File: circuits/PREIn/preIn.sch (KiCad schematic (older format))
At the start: 45 parts, among them K1 CONN_3, P1 CONN_1, P10 CONN_1, P11 CONN_1, P2 CONN_1, P4 CONN_1, P5 CONN_1, P6 CONN_1, P7 CONN_1, P8 CONN_1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

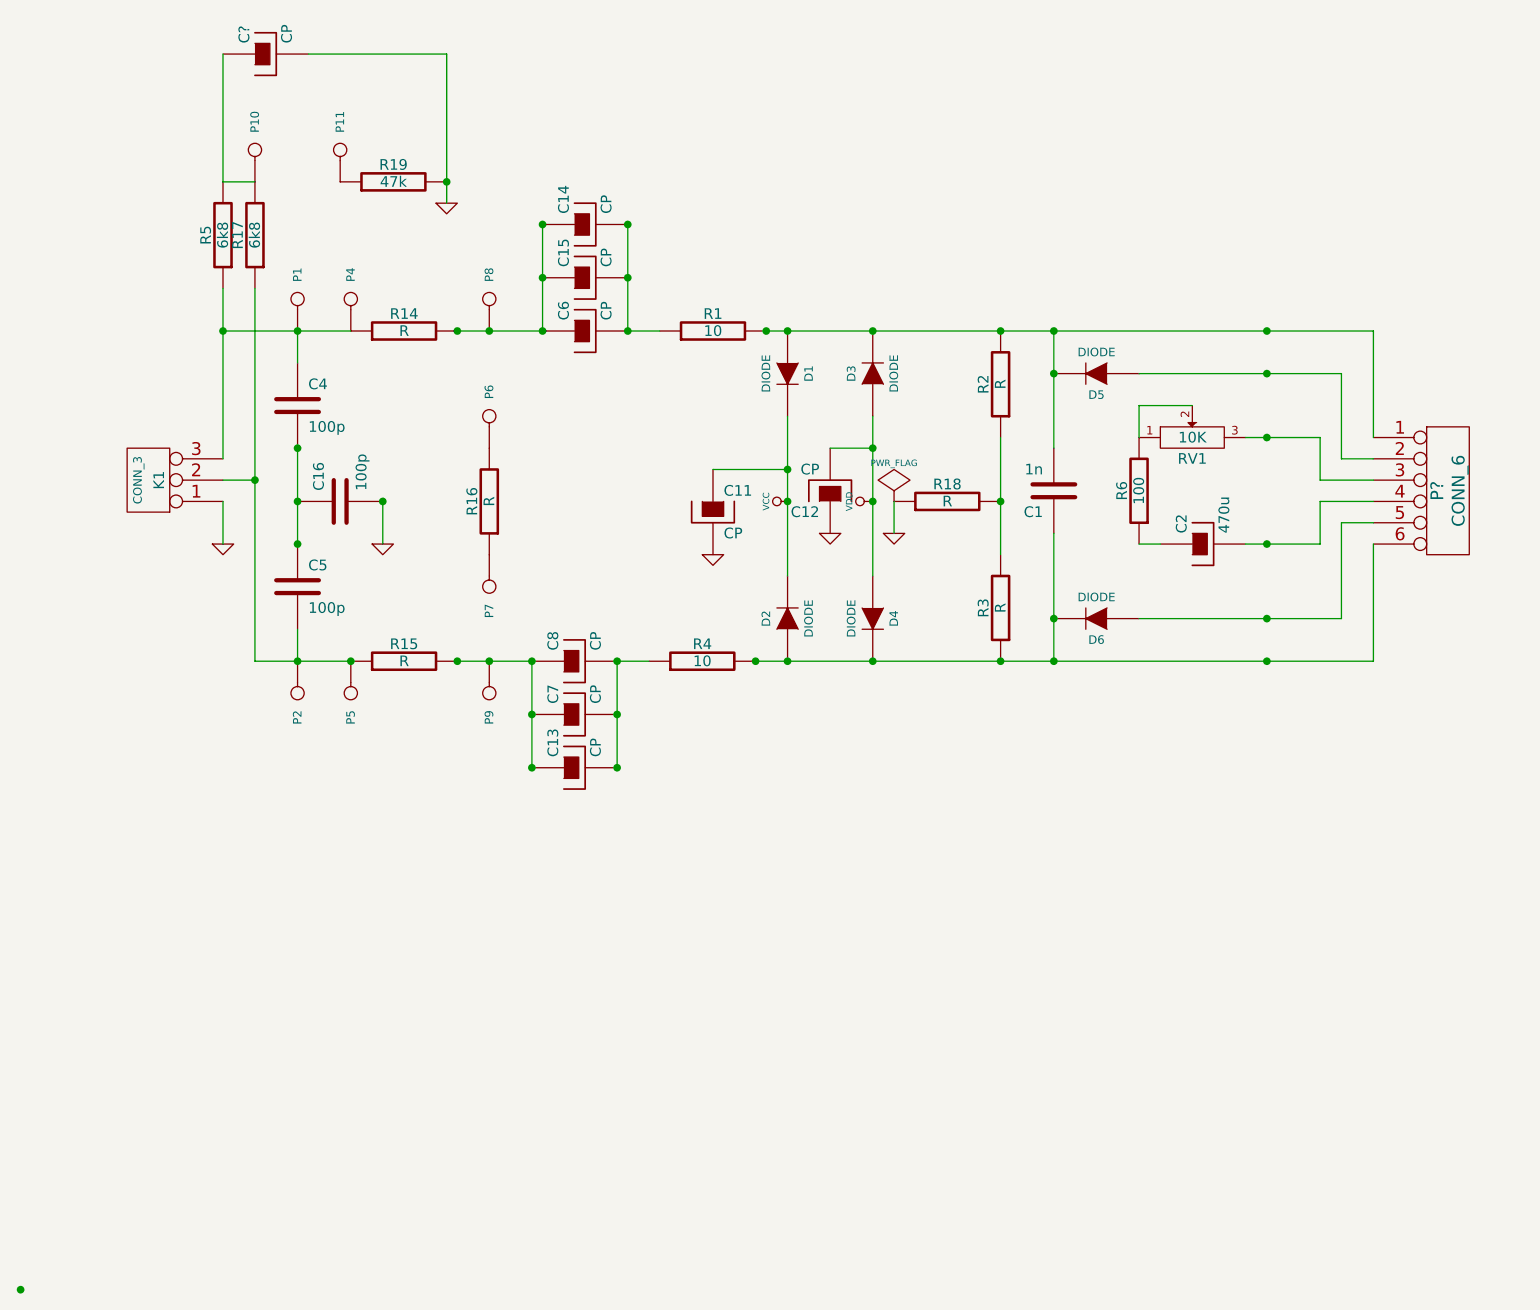
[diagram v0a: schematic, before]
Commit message: docs on transformers
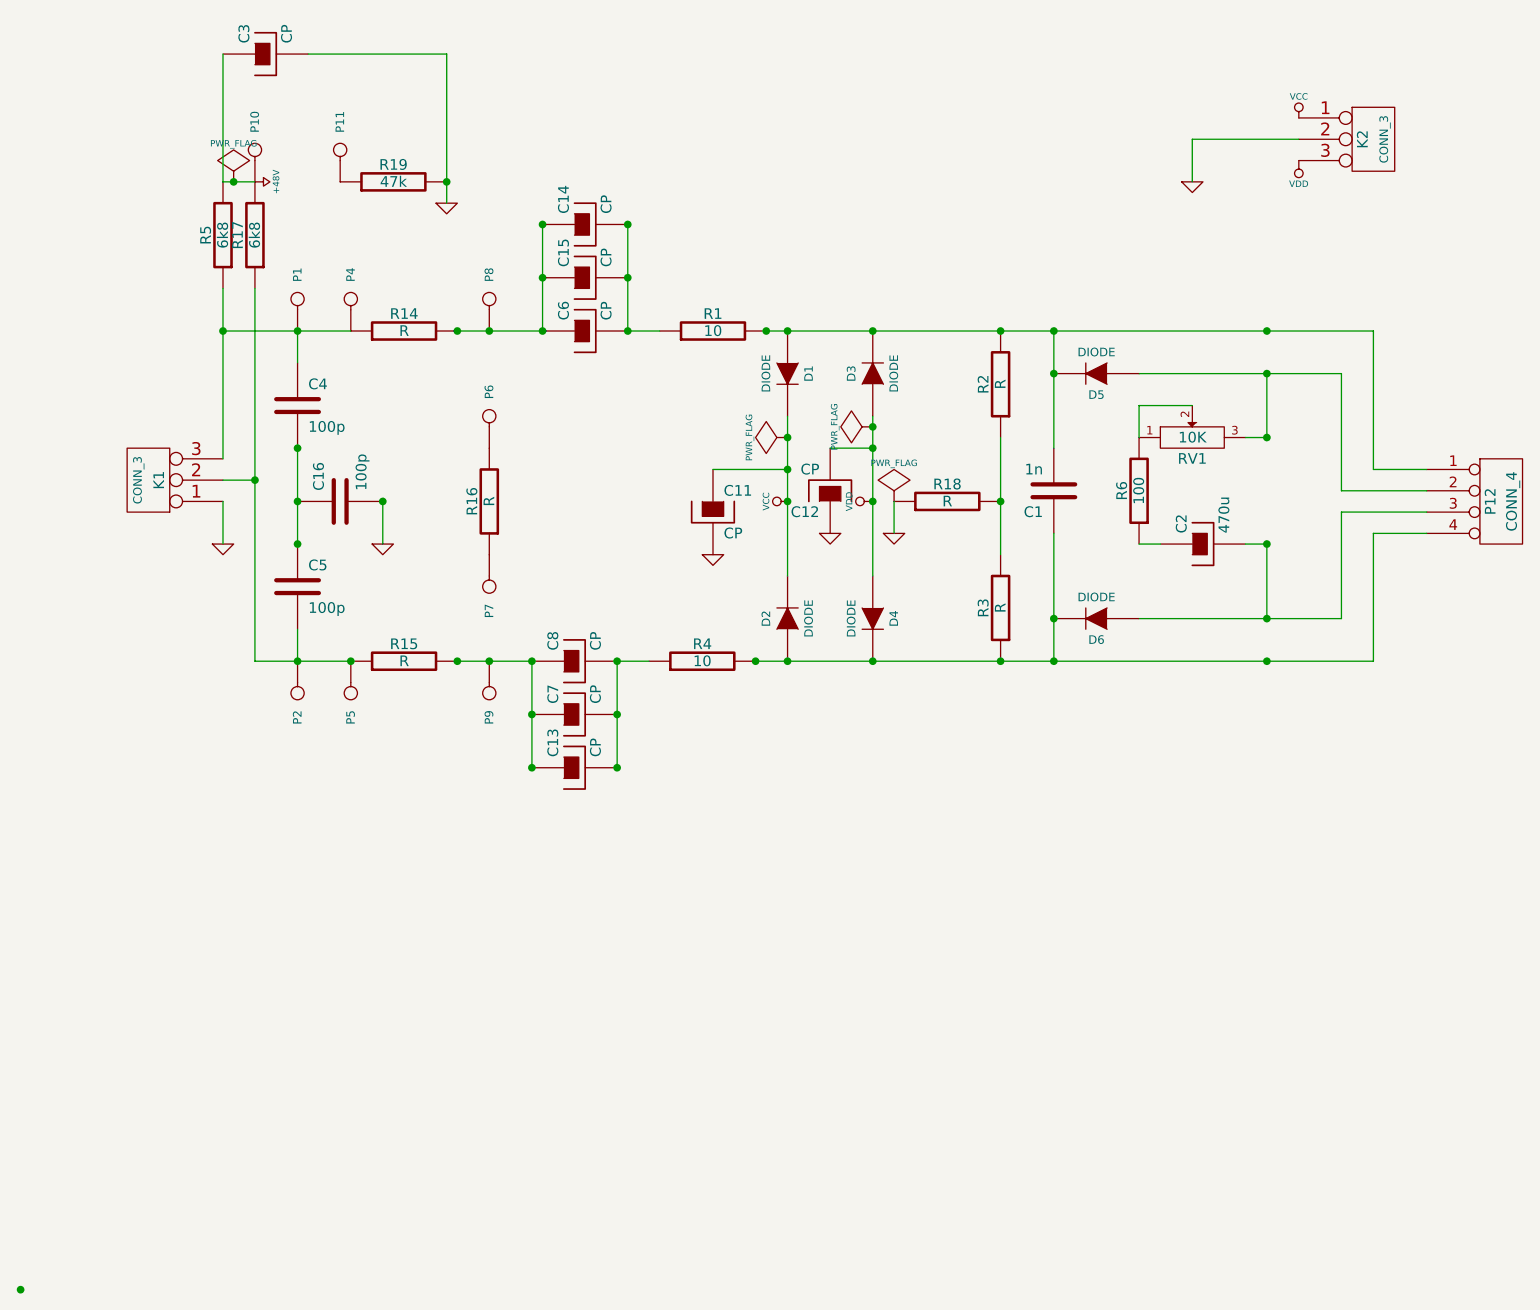
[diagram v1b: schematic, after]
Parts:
- removed P?: CONN_6, symbol CONN_6
- added K2: CONN_3, symbol CONN_3
- added P12: CONN_4, symbol CONN_4
- gave numbers to parts that had none: 1
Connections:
- net GND: now also K2.2 (PM)
- net VCC: now also K2.1 (P1)
- net VDD: now also K2.3 (P3)
- net at C2.2: now also D6.1 (A), P12.3 (P3)
- net at RV1.3: now also D5.1 (A), P12.2 (P2)
- net at C1.1, D2.1 (A), D4.2 (K)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: now also P12.4 (P4)
- net at C1.2, D1.1 (A), D3.2 (K)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: now also P12.1 (P1)
- net +48V: now reaches C3.1, P10.1, R17.2, R5.2
